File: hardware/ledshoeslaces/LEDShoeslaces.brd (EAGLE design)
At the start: 50 x 38 mm, 13 parts, among them IC1 LM1117MPX-5.0

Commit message: fix spacings
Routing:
- net VCC: track 42.5 -> 44.4 mm
- net V_BATT: track 24.7 -> 25.5 mm

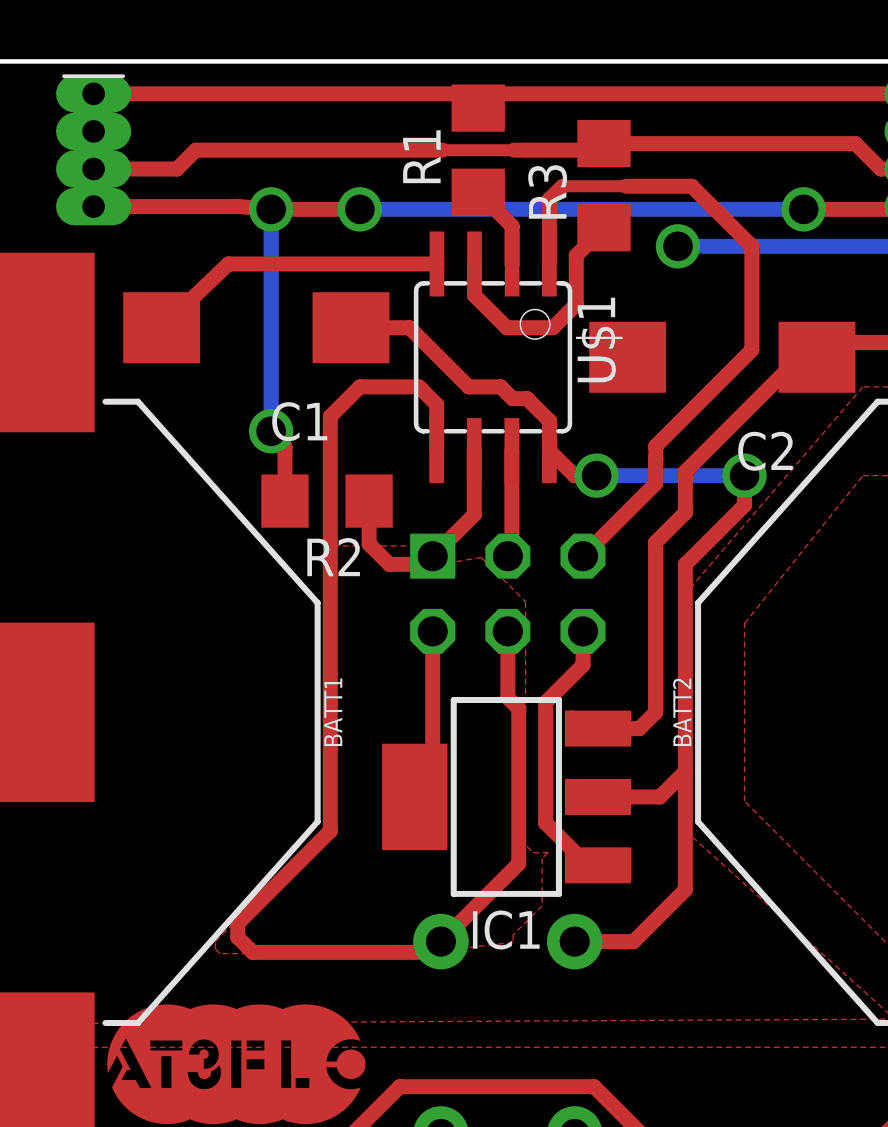
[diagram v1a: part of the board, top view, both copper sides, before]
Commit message: fix minor issues viewed on printed
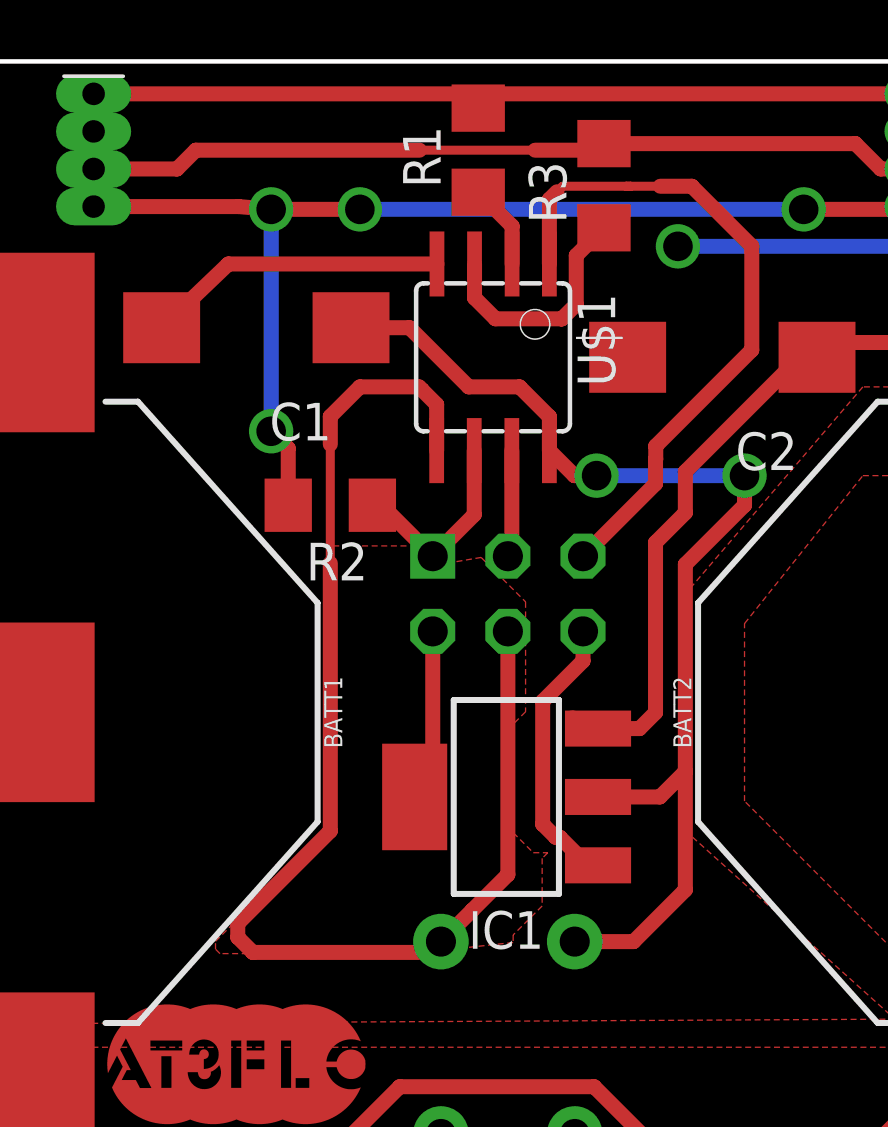
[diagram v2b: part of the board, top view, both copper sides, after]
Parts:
- moved R2 0.18 mm to (19.0, 23.0)
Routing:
- net MISO: track 8.15 -> 6.90 mm

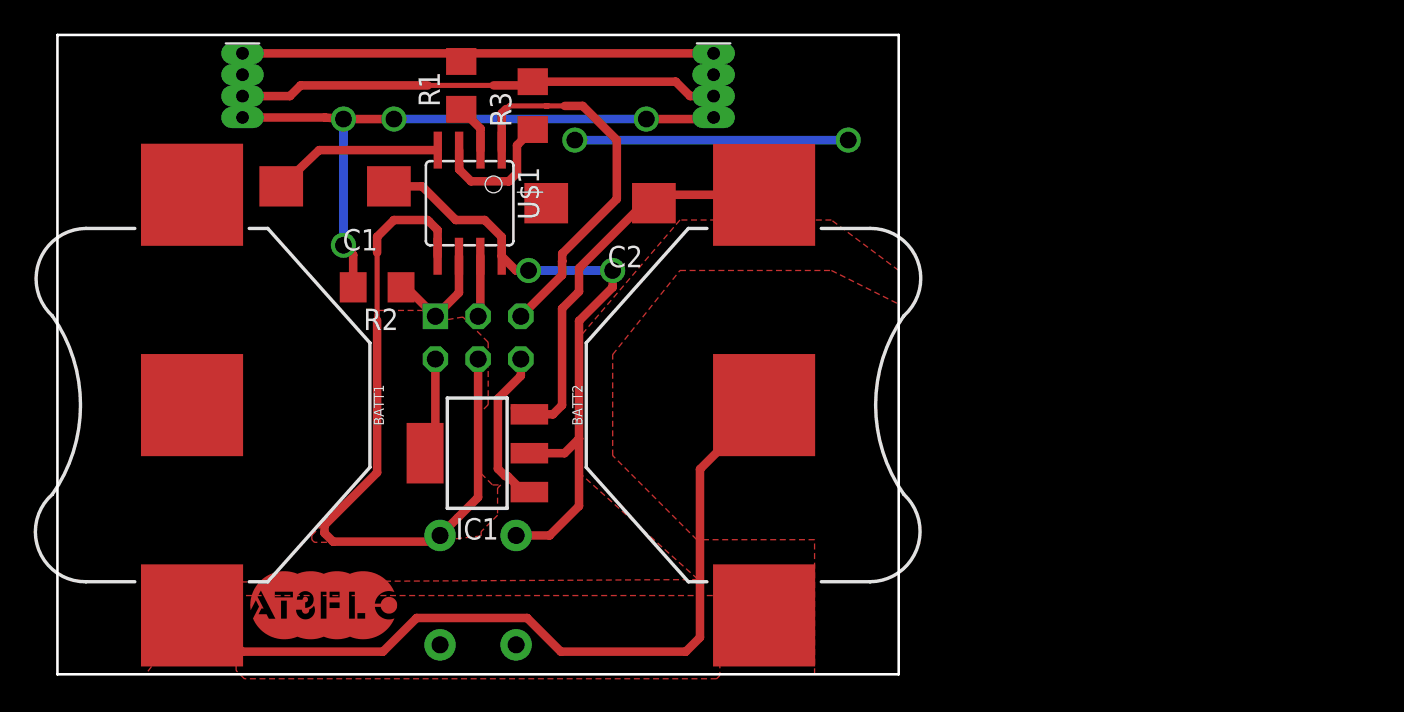
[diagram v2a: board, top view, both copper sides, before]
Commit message: fixing bad led pad
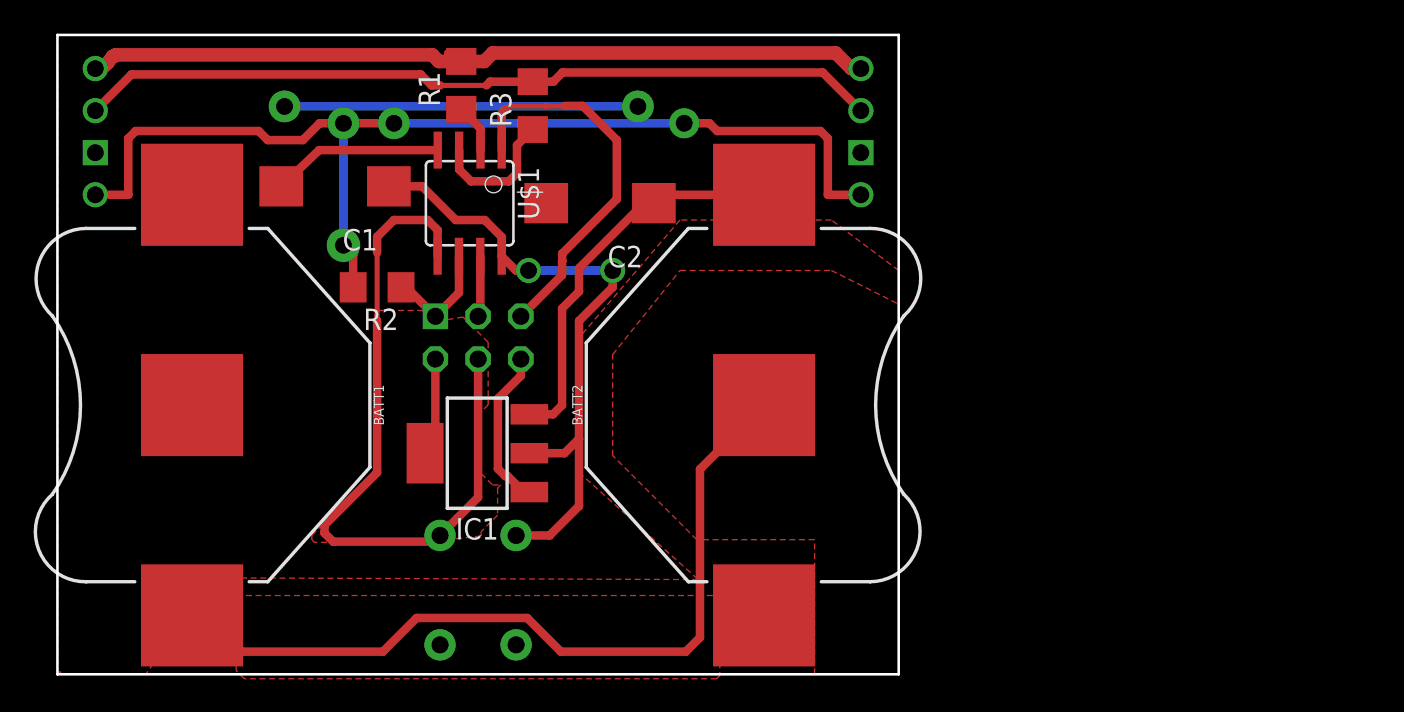
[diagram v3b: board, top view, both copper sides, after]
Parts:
- removed D1, D2: DIFFUSE, SparkFun-LED:LED-RGB-THRU
- added U$3, U$4: LEDRGB, fab:LEDRGB
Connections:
- removed net ABLU: D1.4, D2.4, R2.2
- new net ABLUE: R1.2, U$3.4, U$4.4
- net AGRN: now also U$3.3, U$4.3; no longer D1.3, D2.3
- net ARED: now also R2.2, U$3.1, U$4.1; no longer D1.1, D2.1, R1.2
- net GND: now also U$3.2, U$4.2; no longer D1.2, D2.2
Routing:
- net ABLUE: track 0.00 -> 48.0 mm
- net ABLU: track 38.3 -> 0.00 mm, vias 4 -> 0
- net ARED: track 28.7 -> 63.4 mm, vias 0 -> 4
- net AGRN: track 28.7 -> 47.9 mm
- net GND: track 35.9 -> 40.7 mm
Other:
- board text added: "/ws/ng2017/assets/img/logo-600x600.bmp"
- board text added: "at3flo"

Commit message: zzZZzZZZzzz
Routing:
- net RST: track 23.3 -> 22.6 mm
- added copper zone on layer 1, net MOSI
- added copper zone on layer 1, net V_BATT
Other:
- board text added: "numerik games 2017"
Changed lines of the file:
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@@
 <rectangle x1="0.183940625" y1="0.178859375" x2="0.18859375" y2="0.17928125" layer="1"/>
 <text x="0" y="-0.002115625" size="0.000846875" layer="1" font="vector">/ws/ng2017/assets/img/logo-600x600.bmp</text>
-<text x="13" y="3.75" size="0.000846875" layer="1" font="vector">at3flo</text>
+<text x="13.25" y="3.5" size="0.000846875" layer="1" font="vector">at3flo</text>
+<text x="19.25" y="4.5" size="2" layer="1" font="vector" rot="R180">at3flo</text>
+<text x="78" y="14.25" size="0.000846875" layer="1" font="vector">numerik games 2017</text>
 </plain>
 <attributes>
@@
 <wire x1="28" y1="24" x2="27.2513" y2="24" width="0.508" layer="1"/>
 <wire x1="27.2513" y1="24" x2="26.405" y2="24.8463" width="0.508" layer="1"/>
-<wire x1="28.049" y1="13.14" x2="30.14" y2="13.14" width="0.508" layer="1"/>
-<wire x1="31" y1="14" x2="30.14" y2="13.14" width="0.508" layer="1"/>
 <wire x1="31" y1="14" x2="31" y2="21" width="0.508" layer="1"/>
 <wire x1="27.2606" y1="8.2512" x2="29.2512" y2="8.2512" width="0.508" layer="1"/>
@@
 <wire x1="26.405" y1="24.8463" x2="26.405" y2="25.99261875" width="0.508" layer="1"/>
 <wire x1="26.405" y1="25.99261875" x2="25.39761875" y2="27" width="0.508" layer="1"/>
+<polygon width="0.508" layer="1">
+<vertex x="31.75" y="24"/>
+<vertex x="31.5" y="22.75"/>
+<vertex x="30.5" y="22"/>
+<vertex x="31.25" y="20"/>
+<vertex x="36.5" y="25.75"/>
+<vertex x="34" y="26.5"/>
+</polygon>
+<wire x1="28.049" y1="13.14" x2="30.14" y2="13.14" width="0.508" layer="1"/>
+<wire x1="30.14" y1="13.14" x2="31" y2="14" width="0.508" layer="1"/>
 <wire x1="22.46188125" y1="13.75088125" x2="28.049" y2="13.14" width="0" layer="19" extent="1-1"/>
 </signal>
@@
 <wire x1="25.00188125" y1="18.736903125" x2="25.00188125" y2="10.516296875" width="0.508" layer="1"/>
 <wire x1="19" y1="21.04174375" x2="19" y2="25.0575625" width="0.3048" layer="1"/>
+<polygon width="0.508" layer="1">
+<vertex x="20.75" y="28"/>
+<vertex x="19.5" y="28"/>
+<vertex x="18" y="26.5"/>
+<vertex x="18" y="25.5"/>
+<vertex x="19" y="24.5"/>
+<vertex x="19" y="23.5"/>
+<vertex x="21" y="21.5"/>
+<vertex x="21.5" y="21.5"/>
+<vertex x="23.5" y="23.5"/>
+<vertex x="23.5" y="27.25"/>
+<vertex x="23.25" y="27.5"/>
+<vertex x="21.25" y="27.5"/>
+</polygon>
 </signal>
 <signal name="MISO">
@@
 <wire x1="26.405" y1="31.1543" x2="26.405" y2="33.33755625" width="0.508" layer="1"/>
 <wire x1="26.6620375" y1="33.59459375" x2="26.405" y2="33.33755625" width="0.508" layer="1"/>
-<wire x1="30.151871875" y1="33.7812" x2="31.2188" y2="33.7812" width="0.508" layer="1"/>
-<wire x1="31.2188" y1="33.7812" x2="33.246" y2="31.754" width="0.508" layer="1"/>
-<wire x1="33.246" y1="28.246" x2="30" y2="25" width="0.508" layer="1"/>
+<wire x1="30" y1="25" x2="33.246" y2="28.246" width="0.508" layer="1"/>
 <wire x1="30" y1="25" x2="30" y2="24.559128125" width="0.508" layer="1"/>
 <wire x1="30" y1="24.559128125" x2="29.99199375" y2="24.551121875" width="0.508" layer="1"/>
 <wire x1="29.99199375" y1="24.551121875" x2="29.99199375" y2="23.727015625" width="0.508" layer="1"/>
 <wire x1="29.99199375" y1="23.727015625" x2="27.54188125" y2="21.276903125" width="0.508" layer="1"/>
-<wire x1="33.246" y1="31.754" x2="33.246" y2="28.246" width="0.508" layer="1"/>
 <wire x1="29.15135625" y1="33.7812" x2="29" y2="33.7812" width="0.3048" layer="1"/>
-<wire x1="29.15135625" y1="33.7812" x2="30.151871875" y2="33.7812" width="0.3048" layer="1"/>
+<wire x1="29.965021875" y1="33.7812" x2="29.15135625" y2="33.7812" width="0.3048" layer="1"/>
 <wire x1="29" y1="33.7812" x2="29.15135625" y2="33.7812" width="0.3048" layer="1"/>
 <wire x1="26.84864375" y1="33.7812" x2="26.6620375" y2="33.59459375" width="0.3048" layer="1"/>
 <wire x1="29" y1="33.7812" x2="26.84864375" y2="33.7812" width="0.3048" layer="1"/>
+<wire x1="33.246" y1="28.246" x2="33.246" y2="30.500221875" width="0.508" layer="1"/>
+<wire x1="33.246" y1="30.500221875" x2="29.965021875" y2="33.7812" width="0.508" layer="1"/>
 </signal>
 <signal name="BATS">
@@
 <wire x1="28.049" y1="15.451" x2="29.451" y2="15.451" width="0.508" layer="1"/>
 <wire x1="29.451" y1="15.451" x2="29.992" y2="15.992" width="0.508" layer="1"/>
-<wire x1="29.992" y1="21.738121875" x2="29.992" y2="15.992" width="0.508" layer="1"/>
-<wire x1="29.992" y1="21.738121875" x2="31" y2="22.746121875" width="0.508" layer="1"/>
-<wire x1="31" y1="24.1335875" x2="31" y2="22.746121875" width="0.508" layer="1"/>
+<wire x1="31" y1="23.253325" x2="31" y2="24.1335875" width="0.508" layer="1"/>
+<wire x1="29.992" y1="22.245325" x2="31" y2="23.253325" width="0.508" layer="1"/>
+<wire x1="29.992" y1="15.992" x2="29.992" y2="22.245325" width="0.508" layer="1"/>
+<polygon width="0.508" layer="1">
+<vertex x="36.5" y="28.5"/>
+<vertex x="37.5" y="26.5"/>
+<vertex x="39.5" y="26.5"/>
+<vertex x="39.75" y="28.25"/>
+</polygon>
 </signal>
 <signal name="LEDRED">
